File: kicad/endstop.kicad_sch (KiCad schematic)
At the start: 19 parts, among them U2 SN74LVC07APW

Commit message: Miniaturizing the stepper drivers. They're still too big
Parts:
- C13, C14, C15, C16, C17, C18: footprint Capacitor_SMD:C_0603_1608Metric -> Capacitor_SMD:C_0402_1005Metric
- R10, R11, R12, R13, R6, R7, R8, R9: footprint Resistor_SMD:R_0603_1608Metric -> Resistor_SMD:R_0402_1005Metric
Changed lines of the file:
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@@
 			)
 		)
-		(property "Footprint" "Capacitor_SMD:C_0603_1608Metric"
+		(property "Footprint" "Capacitor_SMD:C_0402_1005Metric"
 			(at 207.9752 81.28 0)
 			(effects
@@
 			)
 		)
-		(property "Footprint" "Capacitor_SMD:C_0603_1608Metric"
+		(property "Footprint" "Capacitor_SMD:C_0402_1005Metric"
 			(at 78.4352 110.49 0)
 			(effects
@@
 			)
 		)
-		(property "Footprint" "Resistor_SMD:R_0603_1608Metric"
+		(property "Footprint" "Resistor_SMD:R_0402_1005Metric"
 			(at 99.06 123.698 90)
 			(effects
@@
 			)
 		)
-		(property "Footprint" "Resistor_SMD:R_0603_1608Metric"
+		(property "Footprint" "Resistor_SMD:R_0402_1005Metric"
 			(at 87.122 106.68 90)
 			(effects
@@
 			)
 		)
-		(property "Footprint" "Capacitor_SMD:C_0603_1608Metric"
+		(property "Footprint" "Capacitor_SMD:C_0402_1005Metric"
 			(at 78.4352 71.12 0)
 			(effects
@@
 			)
 		)
-		(property "Footprint" "Resistor_SMD:R_0603_1608Metric"
+		(property "Footprint" "Resistor_SMD:R_0402_1005Metric"
 			(at 99.06 104.648 90)
 			(effects
@@
 			)
 		)
-		(property "Footprint" "Resistor_SMD:R_0603_1608Metric"
+		(property "Footprint" "Resistor_SMD:R_0402_1005Metric"
 			(at 99.06 84.328 90)
 			(effects
@@
 			)
 		)
-		(property "Footprint" "Capacitor_SMD:C_0603_1608Metric"
+		(property "Footprint" "Capacitor_SMD:C_0402_1005Metric"
 			(at 78.4352 129.54 0)
 			(effects
@@
 			)
 		)
-		(property "Footprint" "Capacitor_SMD:C_0603_1608Metric"
+		(property "Footprint" "Capacitor_SMD:C_0402_1005Metric"
 			(at 220.6752 81.28 0)
 			(effects
@@
 			)
 		)
-		(property "Footprint" "Resistor_SMD:R_0603_1608Metric"
+		(property "Footprint" "Resistor_SMD:R_0402_1005Metric"
 			(at 87.122 125.73 90)
 			(effects
@@
 			)
 		)
-		(property "Footprint" "Resistor_SMD:R_0603_1608Metric"
+		(property "Footprint" "Resistor_SMD:R_0402_1005Metric"
 			(at 87.122 86.36 90)
 			(effects
@@
 			)
 		)
-		(property "Footprint" "Resistor_SMD:R_0603_1608Metric"
+		(property "Footprint" "Resistor_SMD:R_0402_1005Metric"
 			(at 87.122 67.31 90)
 			(effects
@@
 			)
 		)
-		(property "Footprint" "Capacitor_SMD:C_0603_1608Metric"
+		(property "Footprint" "Capacitor_SMD:C_0402_1005Metric"
 			(at 78.4352 90.17 0)
 			(effects
@@
 			)
 		)
-		(property "Footprint" "Resistor_SMD:R_0603_1608Metric"
+		(property "Footprint" "Resistor_SMD:R_0402_1005Metric"
 			(at 99.06 65.278 90)
 			(effects

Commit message: TMC2209->TMC2100, endstop protection optimization
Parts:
- added D2, D3: BAV99S, Package_TO_SOT_SMD:SOT-363_SC-70-6, symbol Diode:BAV99S
- C13, C14, C15, C16, C18: value 0.1uF -> 0.1μF 0402 50V
- C17: value 1 uF -> 0.1μF 0402 50V
- R10, R11, R12, R13: value 100 R -> 10K 0402
- R6, R7, R8, R9: value 100 K -> 100K 0402
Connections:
- net GND: now also D2.1 (A1), D2.4 (A3), D3.1 (A1), D3.4 (A3)
- net Stop A: now also ASTOP1.1 (Pin_1), C16.1, R13.1, R9.1; no longer R13.2
- net Stop X: now also C13.1, R10.1, R6.1, XSTOP1.1 (Pin_1); no longer R10.2
- net Stop Y: now also C14.1, R11.1, R7.1, YSTOP1.1 (Pin_1); no longer R11.2
- net Stop Z: now also C15.1, R12.1, R8.1, ZSTOP1.1 (Pin_1); no longer R12.2
- new net: D3.6 (K3A4), R12.2
- new net: D3.3 (K1A2), R13.2
- new net: D2.3 (K1A2), R11.2
- new net: D2.6 (K3A4), R10.2
- new net +3V3: D2.2 (K2), D2.5 (K4), D3.2 (K2), D3.5 (K4)
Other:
- moved on the sheet: ASTOP1, C13, C14, C15, C16, C17, C18, R6, XSTOP1, YSTOP1, ZSTOP1

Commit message: PCB redo
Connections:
- net +3.3V: no longer C17.1, C18.1, U2.14 (VCC)
- net +3V3: now also C17.1, C18.1, U2.14 (VCC)
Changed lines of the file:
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@@
+	)
+	(symbol
+		(lib_id "power:+3.3V")
+		(at 213.36 69.85 0)
+		(unit 1)
+		(exclude_from_sim no)
+		(in_bom yes)
+		(on_board yes)
+		(dnp no)
+		(property "Reference" "#PWR084"
+			(at 213.36 73.66 0)
+			(effects
+				(font
+					(size 1.27 1.27)
+				)
+				(hide yes)
+			)
+		)
+		(property "Value" "+3V3"
+			(at 213.7283 65.5256 0)
+			(effects
+				(font
+					(size 1.27 1.27)
+				)
+			)
+		)
+		(property "Footprint" ""
+			(at 213.36 69.85 0)
+			(effects
+				(font
+					(size 1.27 1.27)
+				)
+			)
+		)
+		(property "Datasheet" ""
+			(at 213.36 69.85 0)
+			(effects
+				(font
+					(size 1.27 1.27)
+				)
+			)
+		)
+		(property "Description" ""
+			(at 213.36 69.85 0)
+			(effects
+				(font
+					(size 1.27 1.27)
+				)
+				(hide yes)
+			)
+		)
+		(pin "1"
+		)
+		(instances
+			(project "RepHat"
+				(path "/e63e39d7-6ac0-4ffd-8aa3-1841a4541b55/c50ad7f5-975f-4177-af17-0353c7722624"
+					(reference "#PWR084")
+					(unit 1)
+				)
+			)
+		)
 	)
 	(symbol
@@
 					(unit 1)
 				)
-			)
-		)
-	)
-	(symbol
-		(lib_name "+3.3V_2")
-		(lib_id "power:+3.3V")
-		(at 213.36 69.85 0)
-		(unit 1)
-		(exclude_from_sim no)
-		(in_bom yes)
-		(on_board yes)
-		(dnp no)
-		(fields_autoplaced yes)
-		(property "Reference" "#PWR055"
-			(at 213.36 73.66 0)
-			(effects
-				(font
-					(size 1.27 1.27)
-				)
-				(hide yes)
-			)
-		)
-		(property "Value" "+3.3V"
-			(at 213.36 64.77 0)
-			(effects
-				(font
-					(size 1.27 1.27)
-				)
-			)
-		)
-		(property "Footprint" ""
-			(at 213.36 69.85 0)
-			(effects
-				(font
-					(size 1.27 1.27)
-				)
-				(hide yes)
-			)
-		)
-		(property "Datasheet" ""
-			(at 213.36 69.85 0)
-			(effects
-				(font
-					(size 1.27 1.27)
-				)
-				(hide yes)
-			)
-		)
-		(property "Description" ""
-			(at 213.36 69.85 0)
-			(effects
-				(font
-					(size 1.27 1.27)
-				)
-				(hide yes)
-			)
-		)
-		(pin "1"
-		)
-		(instances
-			(project "RepHat"
-				(path "/e63e39d7-6ac0-4ffd-8aa3-1841a4541b55/c50ad7f5-975f-4177-af17-0353c7722624"
-					(reference "#PWR055")
-					(unit 1)
-				)

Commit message: schematic candidate 0
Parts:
- removed R10, R11, R12, R13: 10K 0402, Resistor_SMD:R_0402_1005Metric, symbol Device:R
- added F4: 1A, Fuse:Fuseholder_Littelfuse_Nano2_154x, symbol Device:Fuse
- added RN5: 100R 4x0603, Resistor_SMD:R_Array_Concave_4x0603, symbol Device:R_Pack04
- ASTOP1, XSTOP1, YSTOP1, ZSTOP1: footprint Connector_JST:JST_XH_B3B-XH-A_1x03_P2.50mm_Vertical -> rephat-parts:S3B-XH-SM4-TB
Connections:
- net +3.3V is gone; now on net GND: R6.2, R7.2, R8.2, R9.2
- net +3V3: no longer D2.2 (K2), D2.5 (K4), D3.2 (K2), D3.5 (K4)
- net +5V: now also D2.2 (K2), D2.5 (K4), D3.2 (K2), D3.5 (K4), F4.2; no longer ASTOP1.3 (Pin_3), XSTOP1.3 (Pin_3), YSTOP1.3 (Pin_3), ZSTOP1.3 (Pin_3)
- net Stop A: now also RN5.1 (R1.1); no longer ASTOP1.1 (Pin_1), C16.1, R9.1
- net Stop X: now also RN5.4 (R4.1); no longer C13.1, R6.1, XSTOP1.1 (Pin_1)
- net Stop Y: now also RN5.3 (R3.1); no longer C14.1, R7.1, YSTOP1.1 (Pin_1)
- net Stop Z: now also RN5.2 (R2.1); no longer C15.1, R8.1, ZSTOP1.1 (Pin_1)
- net at D3.6 (K3A4): now also C13.1, R6.1, ZSTOP1.1 (Pin_1), RN5.7 (R2.2)
- net at D3.3 (K1A2): now also ASTOP1.1 (Pin_1), C16.1, R9.1, RN5.8 (R1.2)
- net at D2.3 (K1A2): now also C14.1, R7.1, YSTOP1.1 (Pin_1), RN5.6 (R3.2)
- net at D2.6 (K3A4): now also C15.1, R8.1, XSTOP1.1 (Pin_1), RN5.5 (R4.2)
- new net: ASTOP1.3 (Pin_3), F4.1, XSTOP1.3 (Pin_3), YSTOP1.3 (Pin_3), ZSTOP1.3 (Pin_3)
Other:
- note added: "5V to 3V"
- note added: "Possible things to plug in: - microswitch - hall sensor - inductive probe"
- moved on the sheet: ASTOP1, C16, C17, C18, D2A, D2B, D3A, D3B, R9, U2, XSTOP1, YSTOP1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

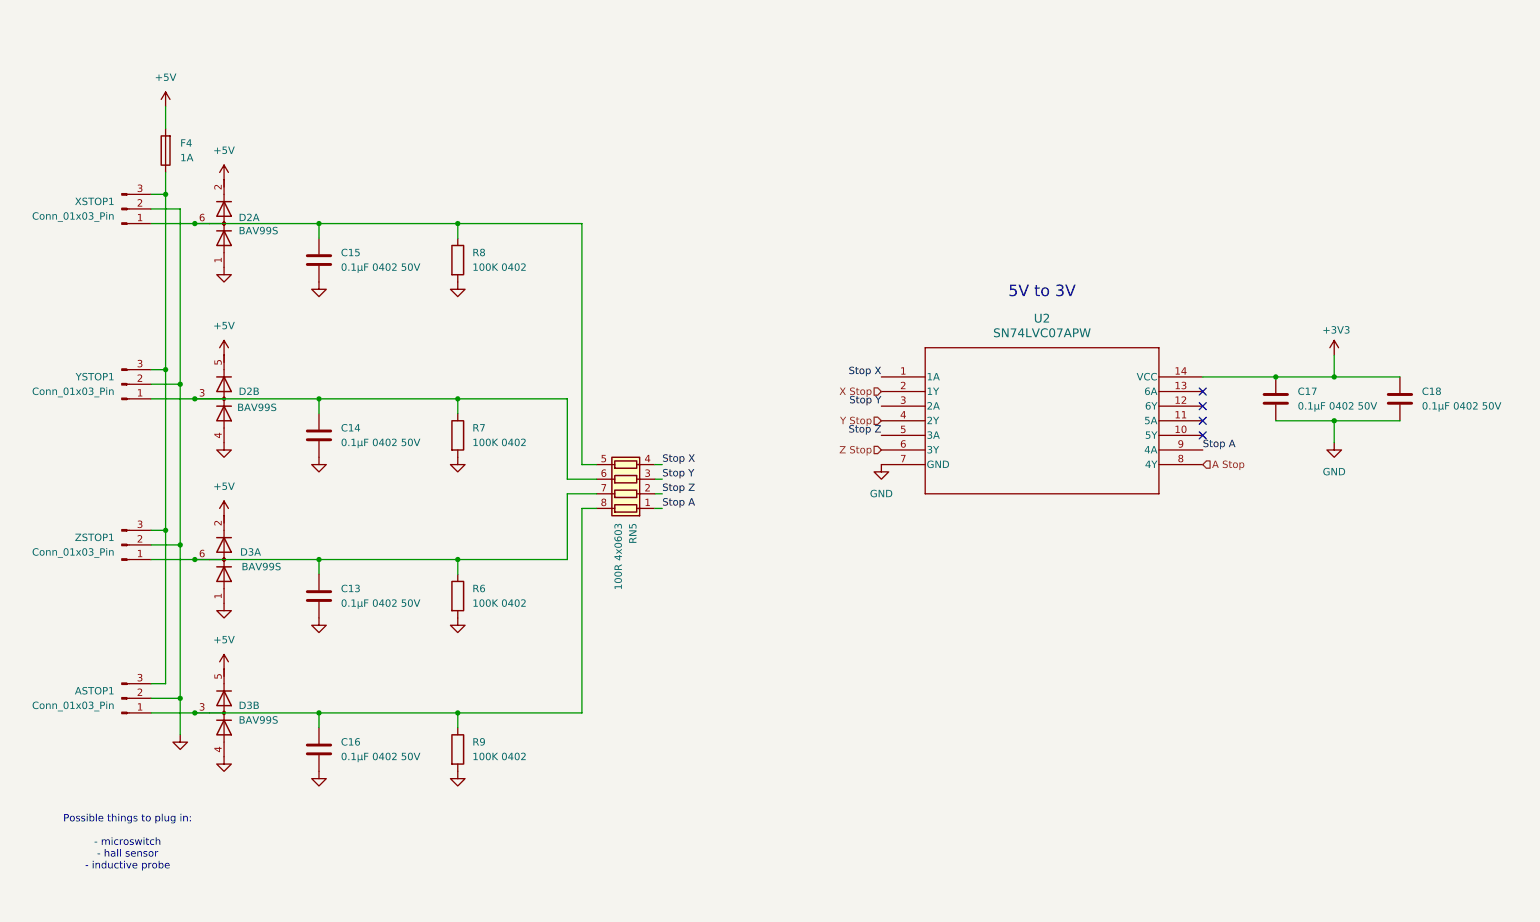
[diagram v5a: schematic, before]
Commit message: new level shifter: bss138 transistors
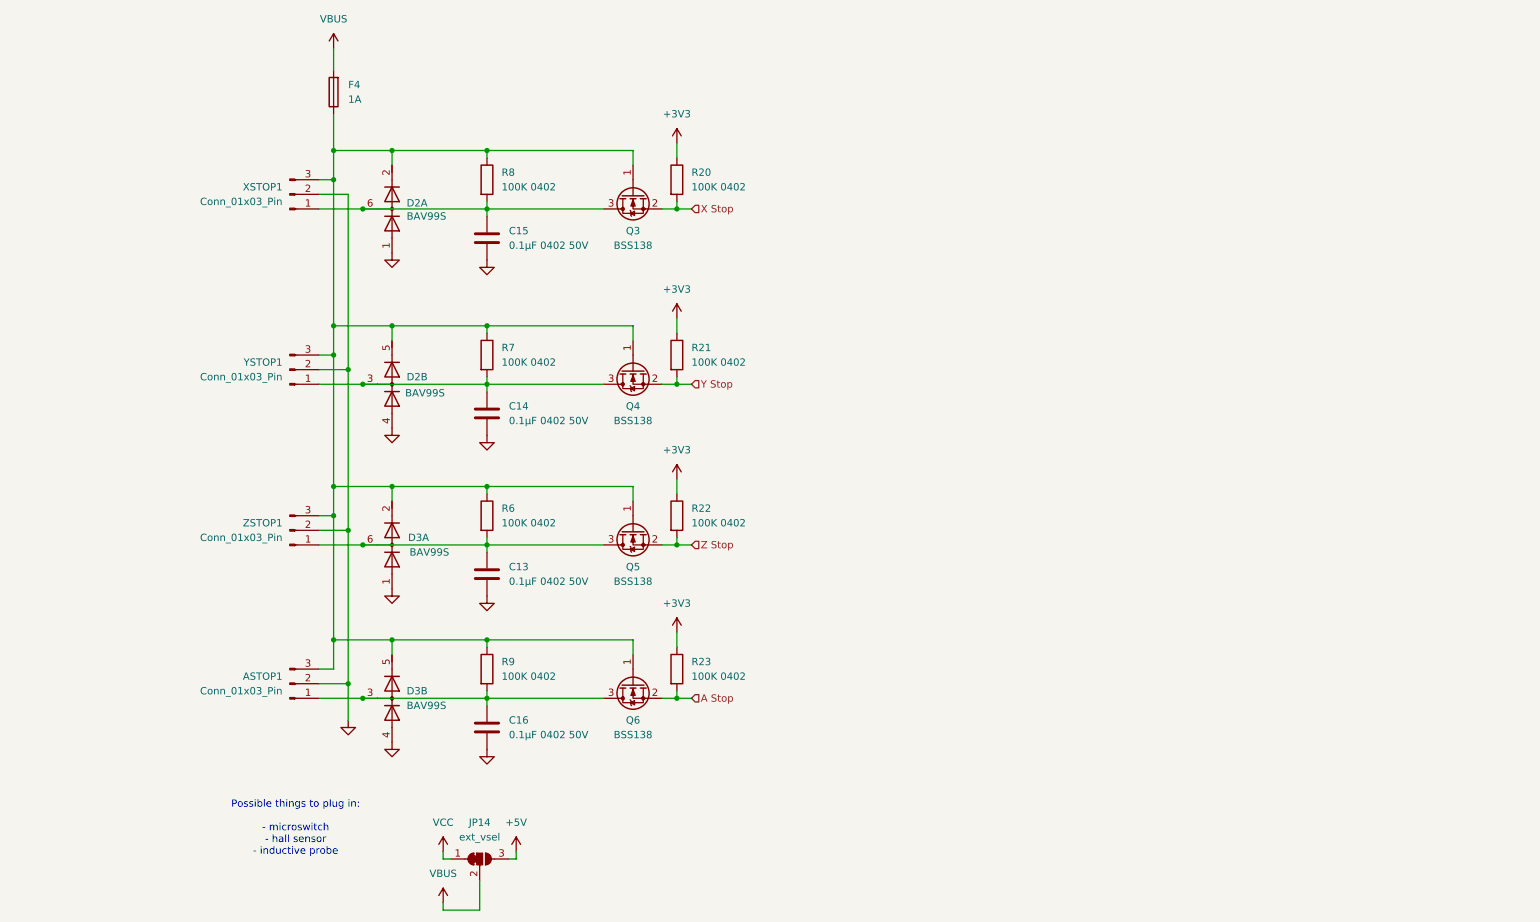
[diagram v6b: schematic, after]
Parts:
- removed C17, C18: 0.1μF 0402 50V, Capacitor_SMD:C_0402_1005Metric, symbol Device:C
- removed RN5: 100R 4x0603, Resistor_SMD:R_Array_Concave_4x0603, symbol Device:R_Pack04
- removed U2: SN74LVC07APW, Package_SO:TSSOP-14-1EP_4.4x5mm_P0.65mm, symbol rephat-symbols:SN74LVC07APW
- added JP14: ext_vsel, Jumper:SolderJumper-3_P1.3mm_Bridged12_RoundedPad1.0x1.5mm, symbol Jumper:SolderJumper_3_Bridged12
- added Q3, Q4, Q5, Q6: BSS138, Package_TO_SOT_SMD:SOT-23, symbol Transistor_FET:BSS138
- added R20, R21, R22, R23: 100K 0402, Resistor_SMD:R_0402_1005Metric, symbol Device:R
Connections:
- net +3V3: now also R20.1, R21.1, R22.1, R23.1
- net +5V: now also JP14.3 (B); no longer D2.2 (K2), D2.5 (K4), D3.2 (K2), D3.5 (K4), F4.2
- net A Stop: now also Q6.2 (S), R23.2
- net GND: no longer R6.2, R7.2, R8.2, R9.2
- net X Stop: now also Q3.2 (S), R20.2
- net Y Stop: now also Q4.2 (S), R21.2
- net Z Stop: now also Q5.2 (S), R22.2
- net at ASTOP1.1 (Pin_1), C16.1, D3.3 (K1A2): now also R9.2, Q6.3 (D); no longer R9.1
- net at C14.1, D2.3 (K1A2), YSTOP1.1 (Pin_1): now also R7.2, Q4.3 (D); no longer R7.1
- net at C15.1, D2.6 (K3A4), XSTOP1.1 (Pin_1): now also R8.2, Q3.3 (D); no longer R8.1
- net at C13.1, D3.6 (K3A4), ZSTOP1.1 (Pin_1): now also R6.2, Q5.3 (D); no longer R6.1
- net at ASTOP1.3 (Pin_3), F4.1, XSTOP1.3 (Pin_3)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: now also D2.2 (K2), D2.5 (K4), D3.2 (K2), D3.5 (K4), R6.1, R7.1, R8.1, R9.1, Q3.1 (G), Q4.1 (G), Q5.1 (G), Q6.1 (G)
- new net VBUS: F4.2, JP14.2 (C)
- new net VCC: JP14.1 (A)
- no-connect marks 4 -> 0
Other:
- note removed: "5V to 3V"
- moved on the sheet: ASTOP1, C13, C14, C15, C16, D2A, D2B, D3A, D3B, F4, R6, R7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

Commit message: schematic finished
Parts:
- removed F4: 1A, Fuse:Fuseholder_Littelfuse_Nano2_154x, symbol Device:Fuse
- added F3: 1812L110 (1.1A), Fuse:Fuse_1812_4532Metric, symbol Device:Polyfuse
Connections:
- net +3V3: now also D2.2 (K2), D2.5 (K4), D3.2 (K2), D3.5 (K4)
- net A Stop: now also D3.3 (K1A2)
- net VBUS: now also F3.2
- net X Stop: now also D2.6 (K3A4)
- net Y Stop: now also D2.3 (K1A2)
- net Z Stop: now also D3.6 (K3A4)
- net at ASTOP1.3 (Pin_3), Q3.1 (G), Q4.1 (G)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: now also F3.1; no longer D2.2 (K2), D2.5 (K4), D3.2 (K2), D3.5 (K4)
- net at C14.1, Q4.3 (D), R7.2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: no longer D2.3 (K1A2)
- net at ASTOP1.1 (Pin_1), C16.1, Q6.3 (D)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: no longer D3.3 (K1A2)
- net at C13.1, Q5.3 (D), R6.2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: no longer D3.6 (K3A4)
- net at C15.1, Q3.3 (D), R8.2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: no longer D2.6 (K3A4)
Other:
- note added: "Possible things to plug in: - microswitch - hall sensor - inductive probe - capacitive probe etc."
- note removed: "Possible things to plug in: - microswitch - hall sensor - inductive probe"
- moved on the sheet: C13, C14, C15, C16, D2A, D2B, D3A, D3B, Q3, Q4, Q5, Q6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
